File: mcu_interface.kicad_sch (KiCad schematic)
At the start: 6 parts, among them U2 MSP430FR2355TPT, Y1 32768

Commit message: Finalized schematic and began assigning footprints
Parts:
- C3, C4: footprint (none) -> Capacitor_SMD:C_0805_2012Metric_Pad1.18x1.45mm_HandSolder
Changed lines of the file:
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@@
       (effects (font (size 1.27 1.27)))
     )
-    (property "Footprint" "" (at 34.29 119.0752 0)
+    (property "Footprint" "Capacitor_SMD:C_0805_2012Metric_Pad1.18x1.45mm_HandSolder" (at 34.29 119.0752 0)
       (effects (font (size 1.27 1.27)) hide)
     )
@@
       (effects (font (size 1.27 1.27)))
     )
-    (property "Footprint" "" (at 34.29 131.7752 0)
+    (property "Footprint" "Capacitor_SMD:C_0805_2012Metric_Pad1.18x1.45mm_HandSolder" (at 34.29 131.7752 0)
       (effects (font (size 1.27 1.27)) hide)
     )

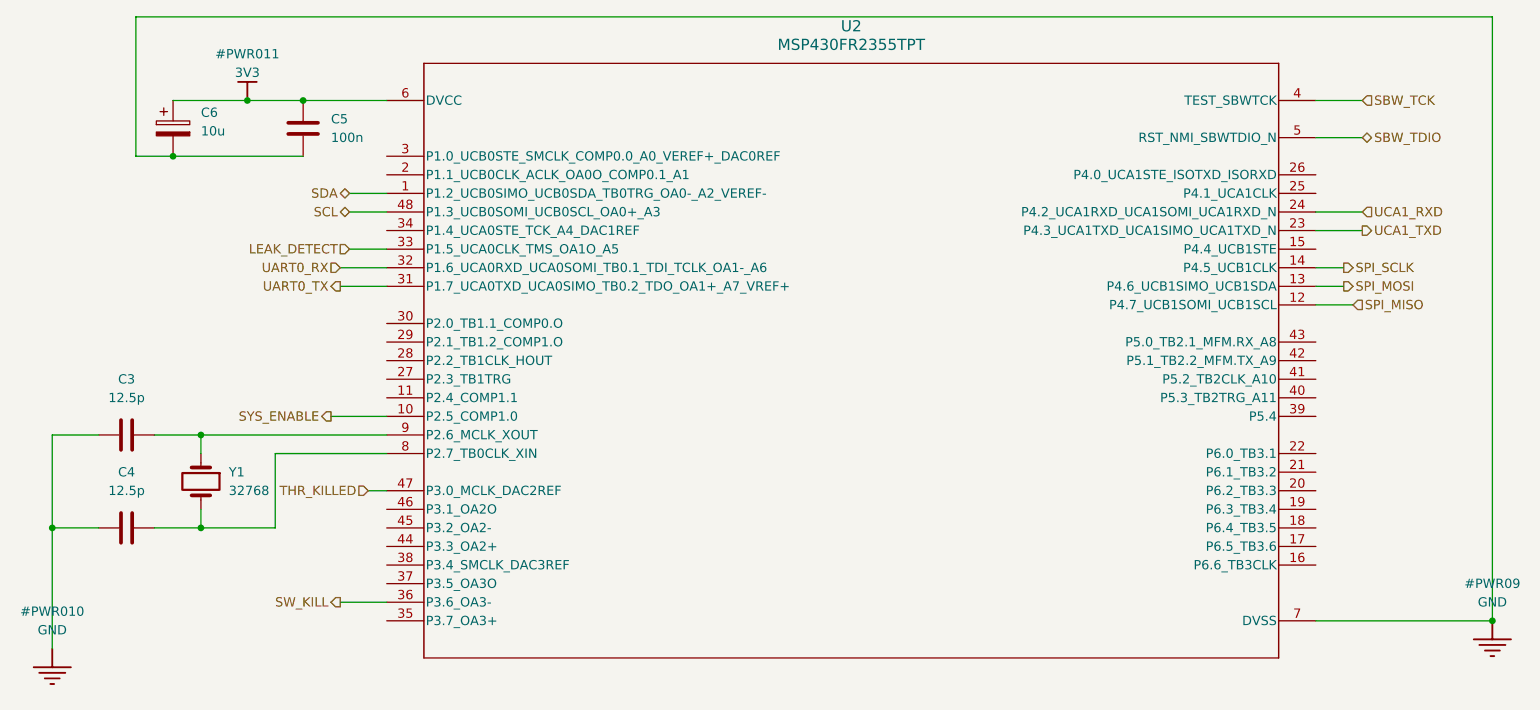
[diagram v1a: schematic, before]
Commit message: updated power and ground symbols in schematic to kicad library version
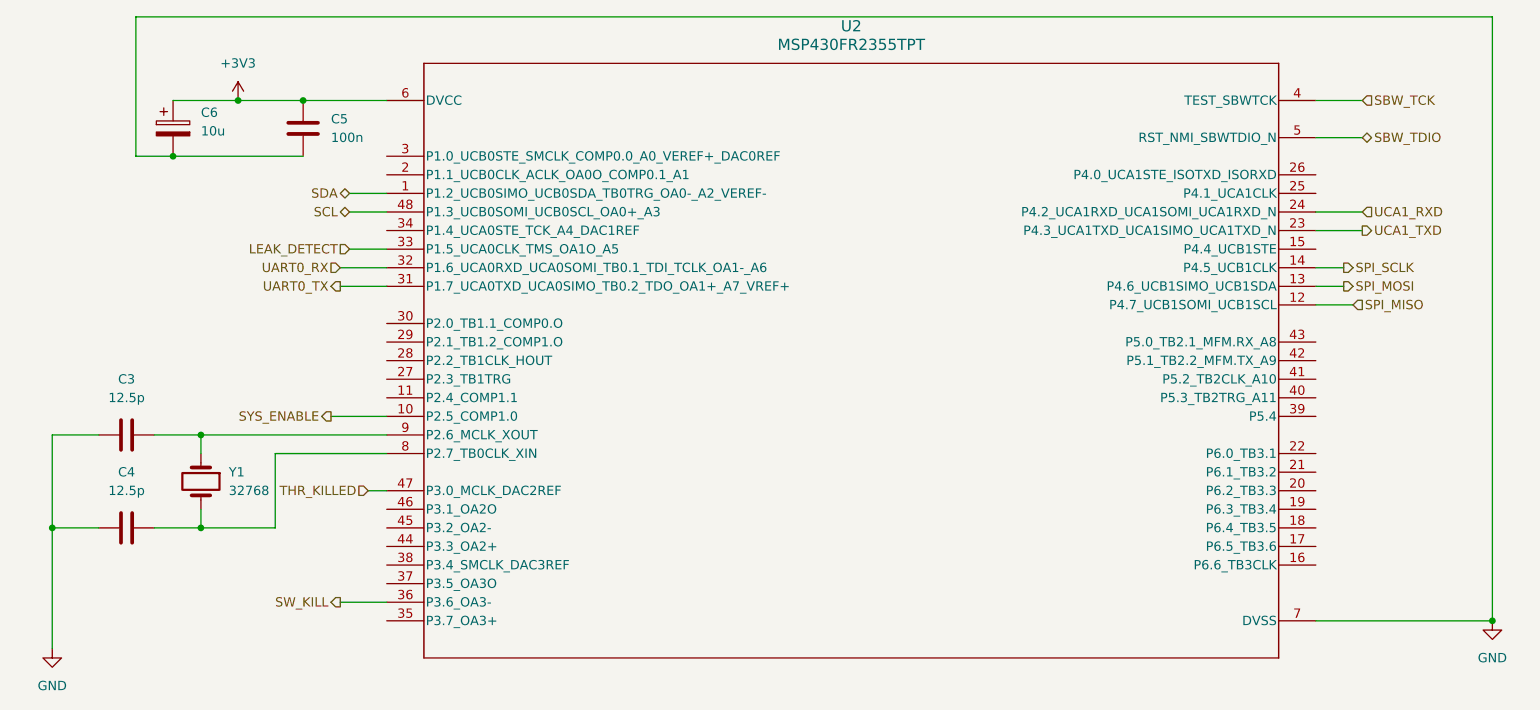
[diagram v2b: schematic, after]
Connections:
- net 3V3 renamed +3V3
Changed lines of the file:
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@@
 (kicad_sch (version 20230121) (generator eeschema)
   (paper "A")
+  (junction (at 53.34 72.39) (diameter 0) (color 0 0 0 0)
+  )
   (junction (at 44.45 80.01) (diameter 0) (color 0 0 0 0)
   )
   (junction (at 48.26 130.81) (diameter 0) (color 0 0 0 0)
   )
-  (junction (at 54.61 72.39) (diameter 0) (color 0 0 0 0)
-  )
   (junction (at 27.94 130.81) (diameter 0) (color 0 0 0 0)
   )
   (junction (at 62.23 72.39) (diameter 0) (color 0 0 0 0)
   )
+  (junction (at 48.26 118.11) (diameter 0) (color 0 0 0 0)
+  )
   (junction (at 224.79 143.51) (diameter 0) (color 0 0 0 0)
   )
-  (junction (at 48.26 118.11) (diameter 0) (color 0 0 0 0)
-  )
   (wire (pts (xy 204.47 95.25) (xy 200.66 95.25))
     (stroke (width 0) (type default))
@@
     (stroke (width 0) (type default))
   )
-  (wire (pts (xy 44.45 72.39) (xy 54.61 72.39))
-    (stroke (width 0) (type default))
-  )
   (wire (pts (xy 200.66 90.17) (xy 207.01 90.17))
     (stroke (width 0) (type default))
   )
+  (wire (pts (xy 53.34 72.39) (xy 62.23 72.39))
+    (stroke (width 0) (type default))
+  )
   (wire (pts (xy 68.58 85.09) (xy 73.66 85.09))
     (stroke (width 0) (type default))
@@
     (stroke (width 0) (type default))
   )
-  (wire (pts (xy 54.61 72.39) (xy 62.23 72.39))
+  (wire (pts (xy 44.45 72.39) (xy 53.34 72.39))
     (stroke (width 0) (type default))
   )
@@
     )
   )
-  (symbol (lib_id "MEB-altium-import:GND") (at 224.79 143.51 0) (unit 1)
-    (in_bom yes) (on_board yes) (dnp no) (fields_autoplaced)
-    (property "Reference" "#PWR09" (at 224.79 138.43 0)
-      (effects (font (size 1.27 1.27)))
-    )
-    (property "Value" "GND" (at 224.79 140.97 0)
-      (effects (font (size 1.27 1.27)))
-    )
-    (property "Footprint" "" (at 224.79 143.51 0)
-      (effects (font (size 1.27 1.27)) hide)
-    )
-    (property "Datasheet" "" (at 224.79 143.51 0)
-      (effects (font (size 1.27 1.27)) hide)
-    )
-    (pin "")
-    (instances
-      (project "MEB"
-        (path "/228e4997-23c1-4c21-939b-583cad26a5e3/33bb8219-dcc3-47e5-a6ab-5e0a1cc34bb1"
-          (reference "#PWR09") (unit 1)
-        )
-      )
-    )
-  )
-  (symbol (lib_id "MEB-altium-import:3V3") (at 54.61 72.39 180) (unit 1)
-    (in_bom yes) (on_board yes) (dnp no)
-    (property "Reference" "#PWR011" (at 54.61 66.04 0)
-      (effects (font (size 1.27 1.27)))
-    )
-    (property "Value" "3V3" (at 54.61 68.58 0)
-      (effects (font (size 1.27 1.27)))
-    )
-    (property "Footprint" "" (at 54.61 72.39 0)
-      (effects (font (size 1.27 1.27)) hide)
-    )
-    (property "Datasheet" "" (at 54.61 72.39 0)
-      (effects (font (size 1.27 1.27)) hide)
-    )
-    (pin "")
-    (instances
-      (project "MEB"
+  (symbol (lib_id "power:GND") (at 27.94 147.32 0) (unit 1)
+    (in_bom yes) (on_board yes) (dnp no) (fields_autoplaced)
+    (property "Reference" "#PWR030" (at 27.94 153.67 0)
+      (effects (font (size 1.27 1.27)) hide)
+    )
+    (property "Value" "GND" (at 27.94 152.4 0)
+      (effects (font (size 1.27 1.27)))
+    )
+    (property "Footprint" "" (at 27.94 147.32 0)
+      (effects (font (size 1.27 1.27)) hide)
+    )
+    (property "Datasheet" "" (at 27.94 147.32 0)
+      (effects (font (size 1.27 1.27)) hide)
+    )
+    (pin "1")
+    (instances
+      (project "MEB"
+        (path "/228e4997-23c1-4c21-939b-583cad26a5e3/3aab6a70-cc66-4393-a750-92acad576aaa"
+          (reference "#PWR030") (unit 1)
+        )
+        (path "/228e4997-23c1-4c21-939b-583cad26a5e3/33bb8219-dcc3-47e5-a6ab-5e0a1cc34bb1"
+          (reference "#PWR010") (unit 1)
+        )
+      )
+    )
+  )
+  (symbol (lib_id "power:+3V3") (at 53.34 72.39 0) (unit 1)
+    (in_bom yes) (on_board yes) (dnp no) (fields_autoplaced)
+    (property "Reference" "#PWR036" (at 53.34 76.2 0)
+      (effects (font (size 1.27 1.27)) hide)
+    )
+    (property "Value" "+3V3" (at 53.34 67.31 0)
+      (effects (font (size 1.27 1.27)))
+    )
+    (property "Footprint" "" (at 53.34 72.39 0)
+      (effects (font (size 1.27 1.27)) hide)
+    )
+    (property "Datasheet" "" (at 53.34 72.39 0)
+      (effects (font (size 1.27 1.27)) hide)
+    )
+    (pin "1")
+    (instances
+      (project "MEB"
+        (path "/228e4997-23c1-4c21-939b-583cad26a5e3"
+          (reference "#PWR036") (unit 1)
+        )
         (path "/228e4997-23c1-4c21-939b-583cad26a5e3/33bb8219-dcc3-47e5-a6ab-5e0a1cc34bb1"
           (reference "#PWR011") (unit 1)
@@
         (path "/228e4997-23c1-4c21-939b-583cad26a5e3/33bb8219-dcc3-47e5-a6ab-5e0a1cc34bb1"
           (reference "C3") (unit 1)
-        )
-      )
-    )
-  )
-  (symbol (lib_id "MEB-altium-import:GND") (at 27.94 147.32 0) (unit 1)
-    (in_bom yes) (on_board yes) (dnp no) (fields_autoplaced)
-    (property "Reference" "#PWR010" (at 27.94 142.24 0)
-      (effects (font (size 1.27 1.27)))
-    )
-    (property "Value" "GND" (at 27.94 144.78 0)
-      (effects (font (size 1.27 1.27)))
-    )
-    (property "Footprint" "" (at 27.94 147.32 0)
-      (effects (font (size 1.27 1.27)) hide)
-    )
-    (property "Datasheet" "" (at 27.94 147.32 0)
-      (effects (font (size 1.27 1.27)) hide)
-    )
-    (pin "")
-    (instances
-      (project "MEB"
-        (path "/228e4997-23c1-4c21-939b-583cad26a5e3/33bb8219-dcc3-47e5-a6ab-5e0a1cc34bb1"
-          (reference "#PWR010") (unit 1)
         )
       )
@@
         )
       )
+    )
+  )
+  (symbol (lib_id "power:GND") (at 224.79 143.51 0) (unit 1)
+    (in_bom yes) (on_board yes) (dnp no) (fields_autoplaced)
+    (property "Reference" "#PWR030" (at 224.79 149.86 0)
+      (effects (font (size 1.27 1.27)) hide)
+    )
+    (property "Value" "GND" (at 224.79 148.59 0)
+      (effects (font (size 1.27 1.27)))
+    )
+    (property "Footprint" "" (at 224.79 143.51 0)
+      (effects (font (size 1.27 1.27)) hide)
+    )
+    (property "Datasheet" "" (at 224.79 143.51 0)
+      (effects (font (size 1.27 1.27)) hide)
+    )
+    (pin "1")
+    (instances
+      (project "MEB"
+        (path "/228e4997-23c1-4c21-939b-583cad26a5e3/3aab6a70-cc66-4393-a750-92acad576aaa"
+          (reference "#PWR030") (unit 1)
+        )
+        (path "/228e4997-23c1-4c21-939b-583cad26a5e3/33bb8219-dcc3-47e5-a6ab-5e0a1cc34bb1"
+          (reference "#PWR09") (unit 1)
+        )
+      )

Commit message: Fix a variety of small issues
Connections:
- net GND: now also C4.1, U2.8 (P2.7_TB0CLK_XIN), Y1.2; no longer C3.2, C4.2
- new net: C3.2, C4.2
- no-connect marks 0 -> 29
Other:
- moved on the sheet: C3, C4, C6
